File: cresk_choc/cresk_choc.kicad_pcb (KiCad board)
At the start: 2 copper layers, 101.8 x 73 mm, 21 parts, among them J1 TRRS, J2 BATTERY, SW1 SW_Push, SW10 SW_Push, SW11 SW_Push, SW12 SW_Push, SW13 SW_Push, SW14 SW_Push, SW15 SW_Push, SW16 SW_Push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

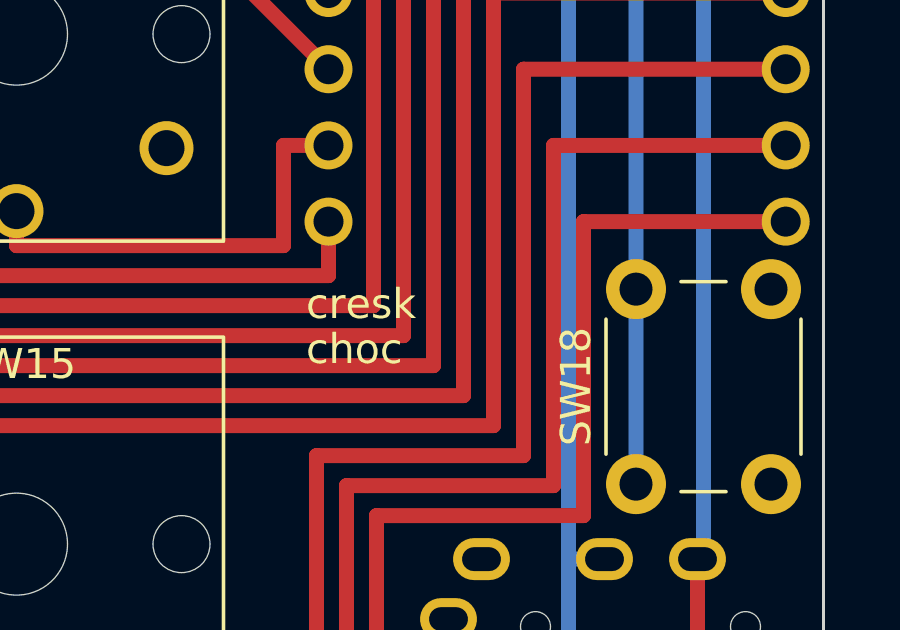
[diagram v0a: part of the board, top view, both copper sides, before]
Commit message: cresk_choc: edit name
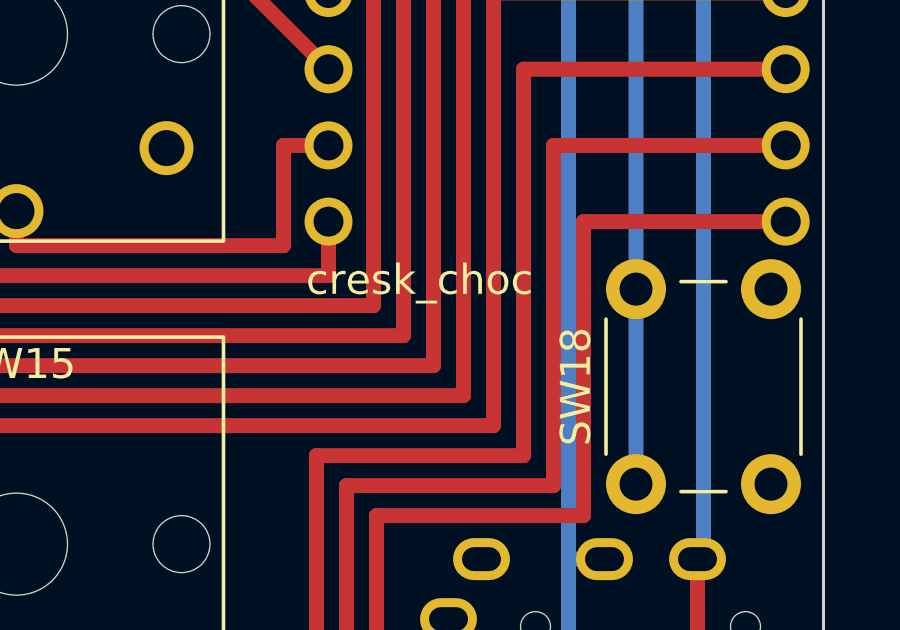
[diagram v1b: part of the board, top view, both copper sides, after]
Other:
- board text added: "cresk_choc"
- board text removed: "choc"
- board text removed: "cresk"
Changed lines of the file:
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@@
   (gr_arc (start 76.5 95.5) (mid 75.914214 96.914214) (end 74.5 97.5) (layer "Edge.Cuts") (width 0.1))
   (gr_arc (start 44.1 61.5) (mid 44.685786 60.085786) (end 46.1 59.5) (layer "Edge.Cuts") (width 0.1))
-  (gr_text "choc" (at 128.65 82.5) (layer "F.SilkS")
+  (gr_text "cresk_choc\n " (at 128.65 81) (layer "F.SilkS")
     (effects (font (size 1 1) (thickness 0.15)) (justify left))
   )
-  (gr_text "cresk" (at 128.65 81) (layer "F.SilkS")
-    (effects (font (size 1 1) (thickness 0.15)) (justify left))
-  )
